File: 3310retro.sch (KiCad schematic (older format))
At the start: 10 parts

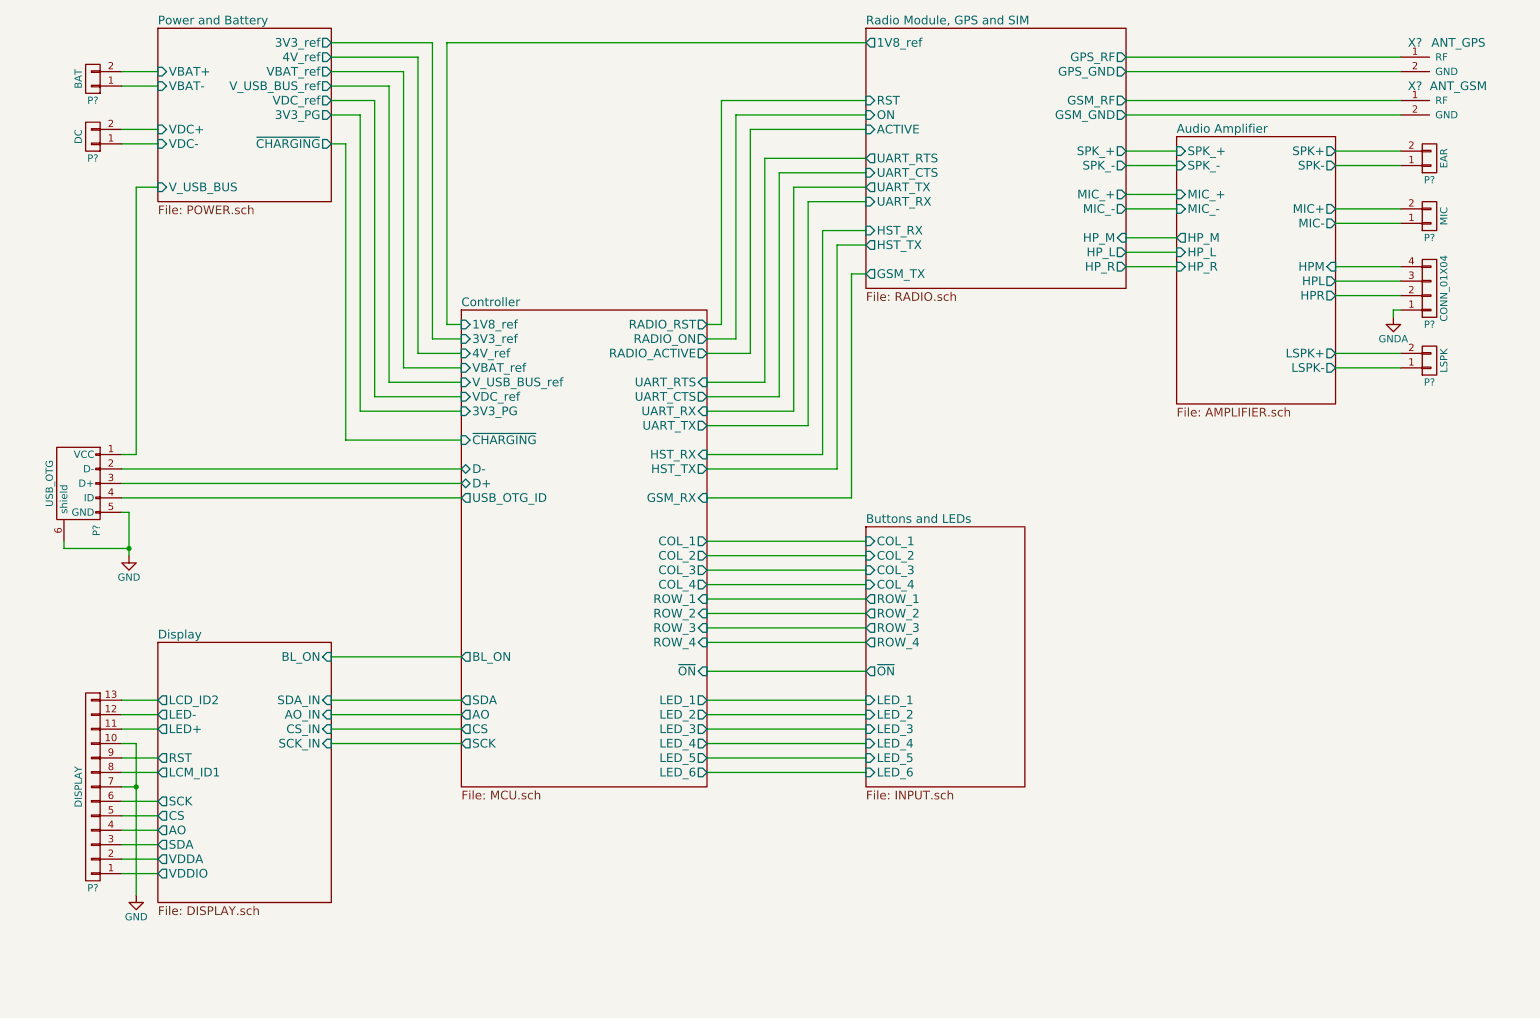
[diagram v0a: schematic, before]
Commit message: Schematics:  - Added STZM32 MCU for the CPU kernel  - Added ESP8266 for WiFi Subsheet
Firmware:
 - Generated BIOS configuration for CubeMX
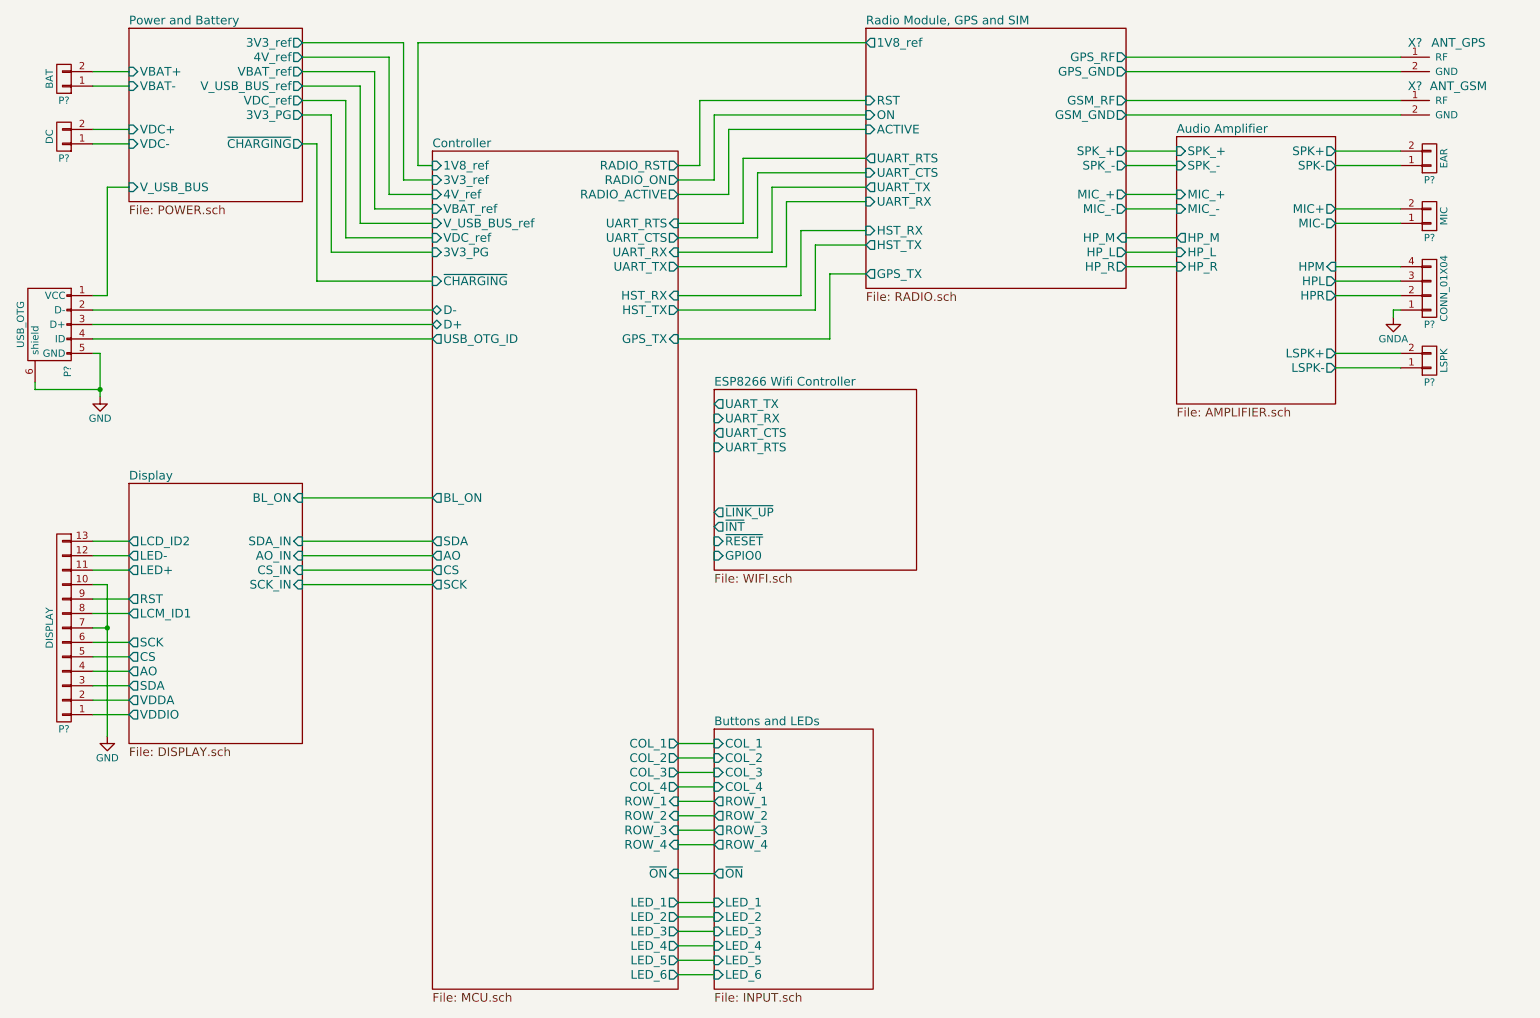
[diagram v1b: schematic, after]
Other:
- moved on the sheet: P?

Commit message: current version of the schematics. Audio circuits are still missing.
Audio curcuit topology
Audio from cellphone module is routed to STM
Audio from microphone is routed to STM
STM processes audio and routes microphone data to cellphone module
STM processes audio and routes cellphone audio to amplifier
analog multiplexer can switch route from mic directly to cellphone module and module to speaker
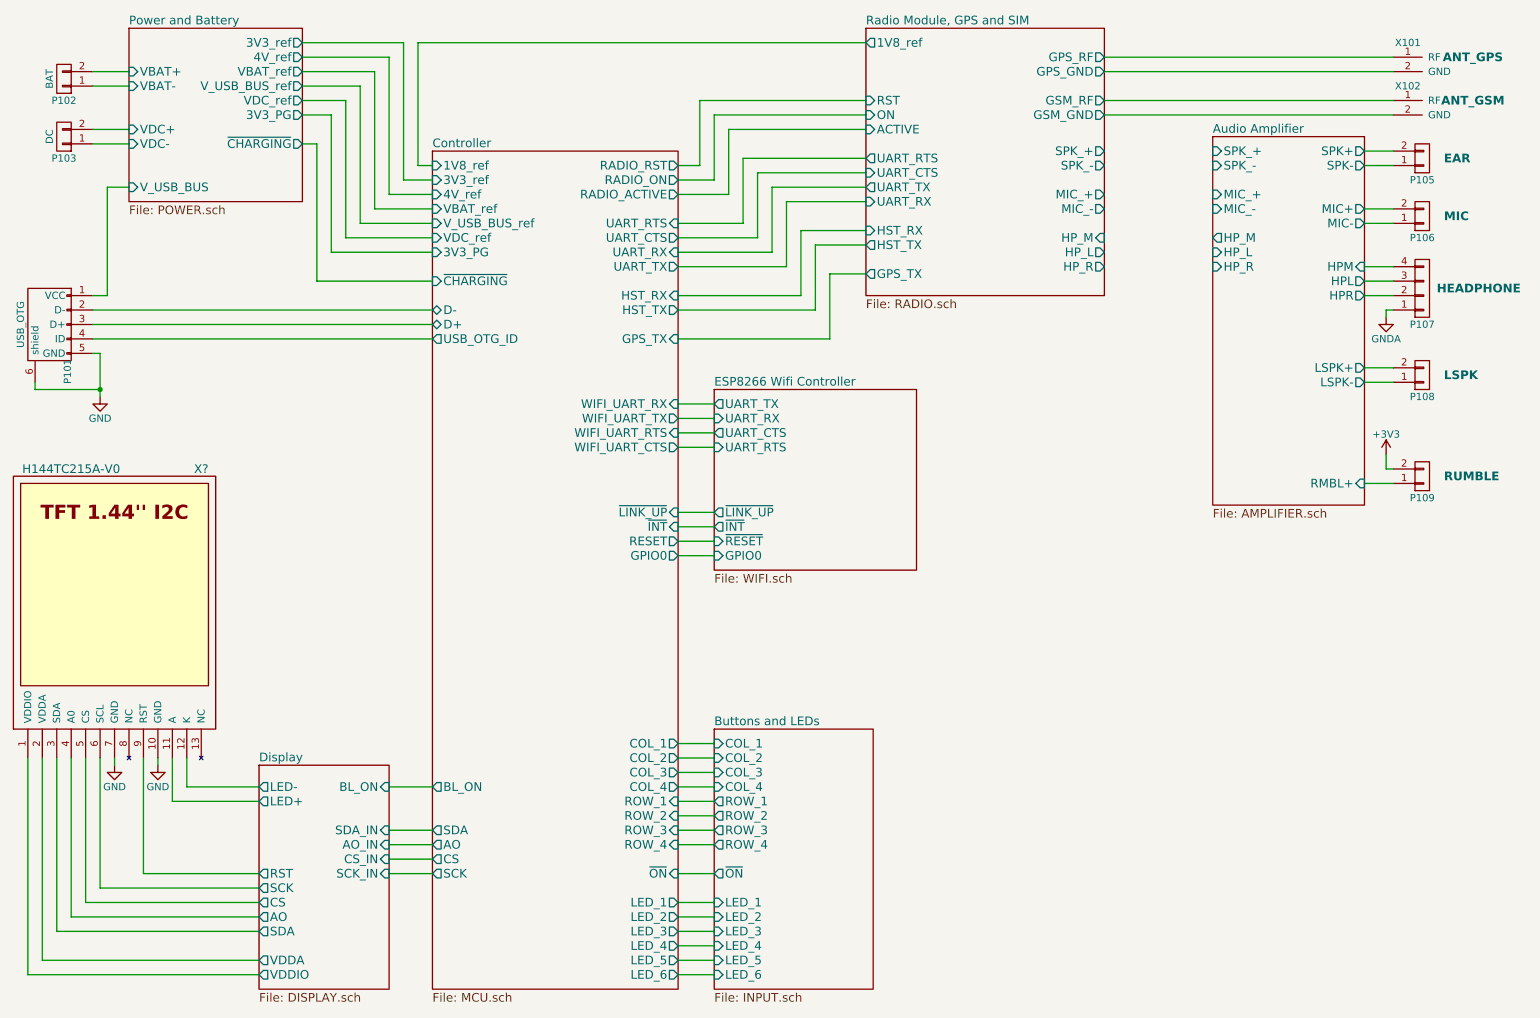
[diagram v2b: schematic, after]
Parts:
- removed P?: DISPLAY, symbol CONN_01X13
- added P109: RUMBLE, buttons:Rumble_Pads, symbol CONN_01X02
- added X?: H144TC215A-V0, symbol H144TC215A-V0
- P107: renamed from P?; value CONN_01X04 -> HEADPHONE
- gave numbers to parts that had none: 8
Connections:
- net Display/AO: now also X?.4 (A0)
- net Display/CS: now also X?.5 (CS)
- net Display/LED+: now also X?.11 (A)
- net Display/LED-: now also X?.12 (K)
- net Display/RST: now also X?.9 (RST)
- net Display/SCK: now also X?.6 (SCL)
- net Display/SDA: now also X?.3 (SDA)
- net Display/VDDA: now also X?.2 (VDDA)
- net Display/VDDIO: now also X?.1 (VDDIO)
- net GND: now also X?.10 (GND), X?.7 (GND)
- new net +3V3: P109.2 (P2)
- new net Audio Amplifier/RMBL+: P109.1 (P1)
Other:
- moved on the sheet: P105, P106, P107, P108, X101, X102
